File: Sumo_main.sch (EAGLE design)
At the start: 52 parts, among them IC1 TL331, U1 ATMEGA8U2AU, U2 SN65HVD3082, U3 LM339D, X2 RS485, Y1 16MHz

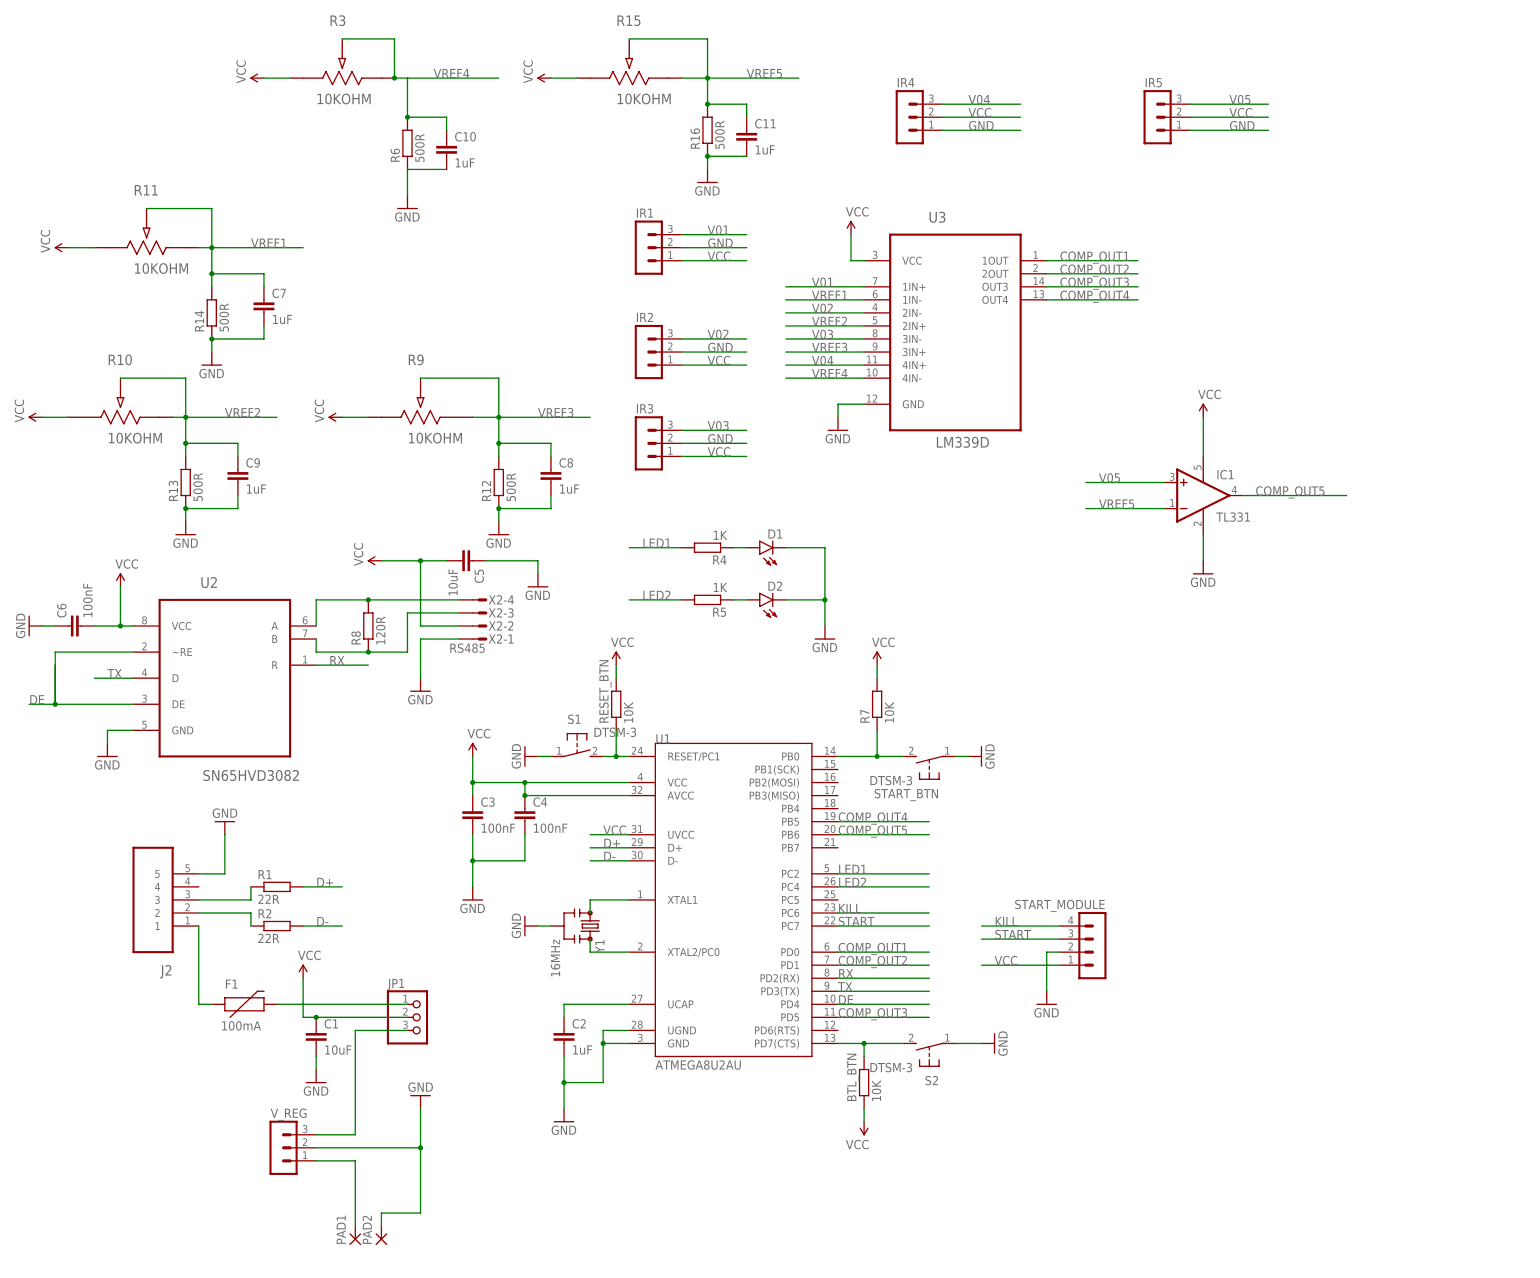
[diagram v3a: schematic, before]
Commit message: Add line sensor to schematic.
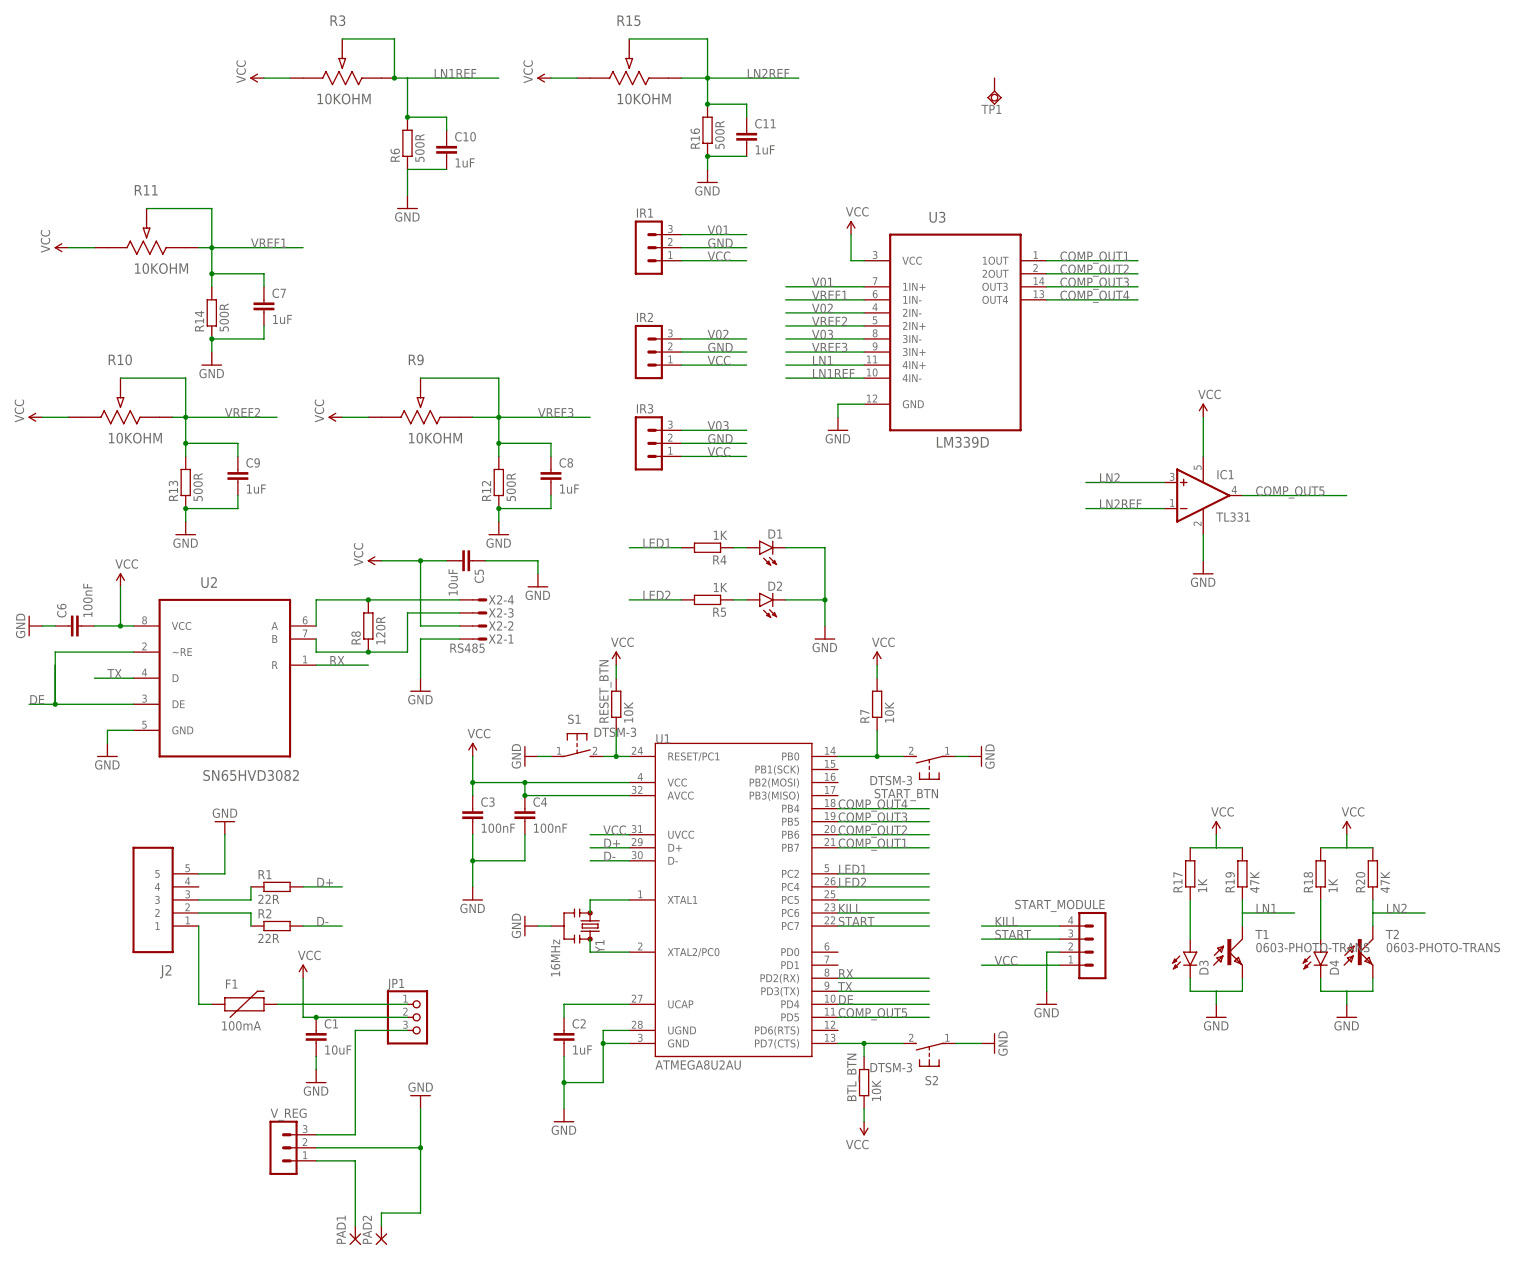
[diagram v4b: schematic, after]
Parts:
- removed IR4, IR5: (no value), con-lstb:MA03-1
- added D3, D4: (no value), SparkFun-LED:LED0603
- added R17, R18: 1K, resistor:R-EU_R0603
- added R19, R20: 47K, resistor:R-EU_R0603
- added T1, T2: 0603-PHOTO-TRANS, Phototransistor 0603:0603-PHOTO-TRANS
- added TP1: TPSQTP08SQ, testpad:TPSQTP08SQ
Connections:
- net VREF4 renamed LN1REF
- net VREF5 renamed LN2REF
- removed net V04: IR4.3, U3.4IN+
- removed net V05: IC1.+IN, IR5.3
- new net LN1: R19.1, T1.C, U3.4IN+
- new net LN2: IC1.+IN, R20.1, T2.C
- new net N$15: D3.A, R17.1
- new net N$17: U1.PC5
- new net N$18: D4.A, R18.1
- net COMP_OUT1: now also U1.PB7; no longer U1.PD0
- net COMP_OUT2: now also U1.PB6; no longer U1.PD1
- net COMP_OUT3: now also U1.PB5; no longer U1.PD5
- net COMP_OUT4: now also U1.PB4; no longer U1.PB5
- net COMP_OUT5: now also U1.PD5; no longer U1.PB6
- net GND: now also D3.C, D4.C, IR2.2, T1.E, T2.E; no longer IR4.1, IR5.1
- net VCC: now also R17.2, R18.2, R19.2, R20.2; no longer IR4.2, IR5.2

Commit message: Remove unnecessary components that are moved to other board.
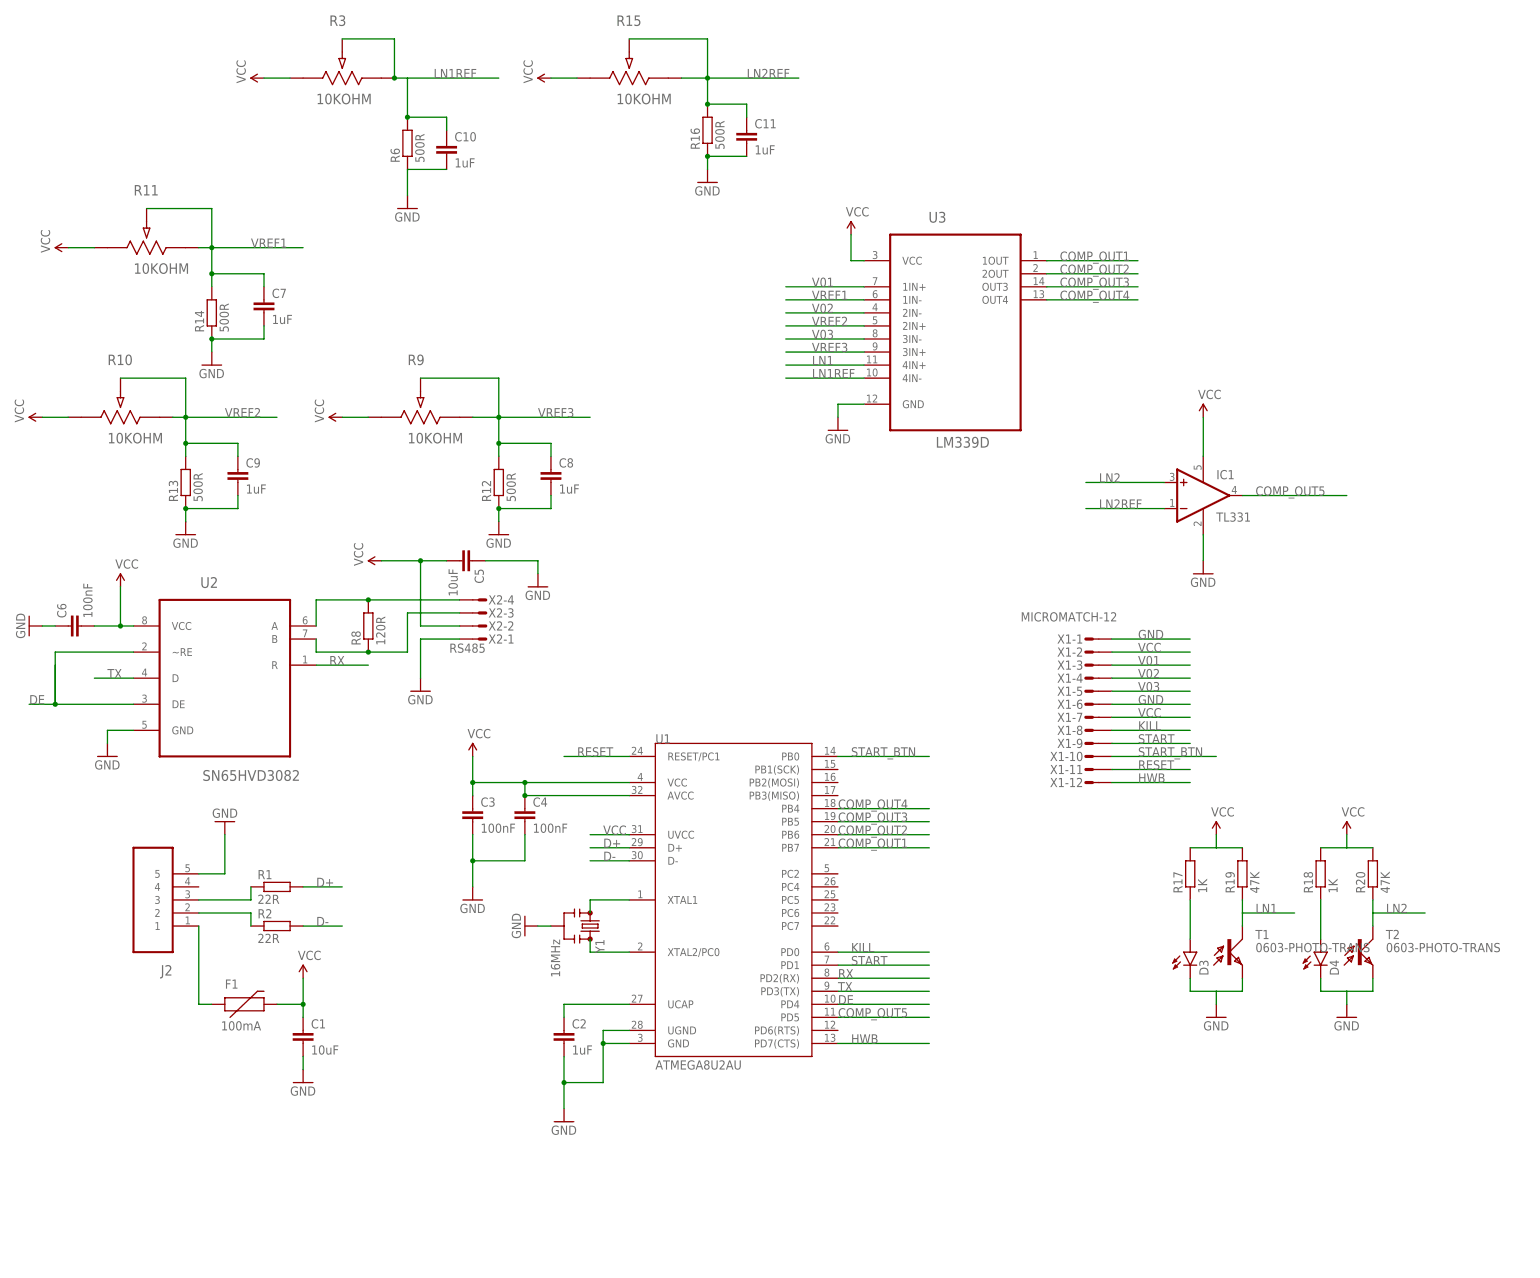
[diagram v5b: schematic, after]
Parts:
- removed BTL_BTN, R7, RESET_BTN: 10K, resistor:R-EU_R0603
- removed D1, D2: (no value), SparkFun-LED:LED0603
- removed IR1, IR2, IR3, V_REG: (no value), con-lstb:MA03-1
- removed JP1: (no value), pinhead:PINHD-1X3
- removed PAD1, PAD2: (no value), wirepad:2,15/1,0
- removed R4, R5: 1K, resistor:R-EU_R0603
- removed S1, S2, START_BTN: DTSM-3, switch-tact:DTSM-3
- removed START_MODULE: (no value), con-lstb:MA04-1
- removed TP1: TPSQTP08SQ, testpad:TPSQTP08SQ
- added X1: MICROMATCH-12, con-amp-micromatch:MICROMATCH-12
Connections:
- removed net LED1: R4.2, U1.PC2
- removed net LED2: R5.2, U1.PC4
- removed net N$10: D1.A, R4.1
- removed net N$12: F1.2, JP1.1
- removed net N$13: BTL_BTN.2, S2.2, U1.PD7(CTS)
- removed net N$14: JP1.3, V_REG.3
- removed net N$17: U1.PC5
- removed net N$23: PAD1.P, V_REG.1
- removed net N$4: RESET_BTN.1, S1.2, U1.RESET/PC1
- removed net N$8: R7.1, START_BTN.2, U1.PB0
- removed net N$9: D2.A, R5.1
- new net HWB: U1.PD7(CTS), X1-12.S
- new net RESET: U1.RESET/PC1, X1-11.S
- new net START_BTN: U1.PB0, X1-10.S
- net GND: now also X1-1.S, X1-6.S; no longer D1.C, D2.C, IR1.2, IR2.2, IR3.2, PAD2.P, S1.1, S2.1, START_BTN.1, START_MODULE.2, V_REG.2
- net KILL: now also U1.PD0, X1-8.S; no longer START_MODULE.4, U1.PC6
- net START: now also U1.PD1, X1-9.S; no longer START_MODULE.3, U1.PC7
- net V01: now also X1-3.S; no longer IR1.3
- net V02: now also X1-4.S; no longer IR2.3
- net V03: now also X1-5.S; no longer IR3.3
- net VCC: now also F1.2, X1-2.S, X1-7.S; no longer BTL_BTN.1, IR1.1, IR2.1, IR3.1, JP1.2, R7.2, RESET_BTN.2, START_MODULE.1
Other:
- moved on the sheet: C1

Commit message: Finish and fix errors of Main's schematic and board
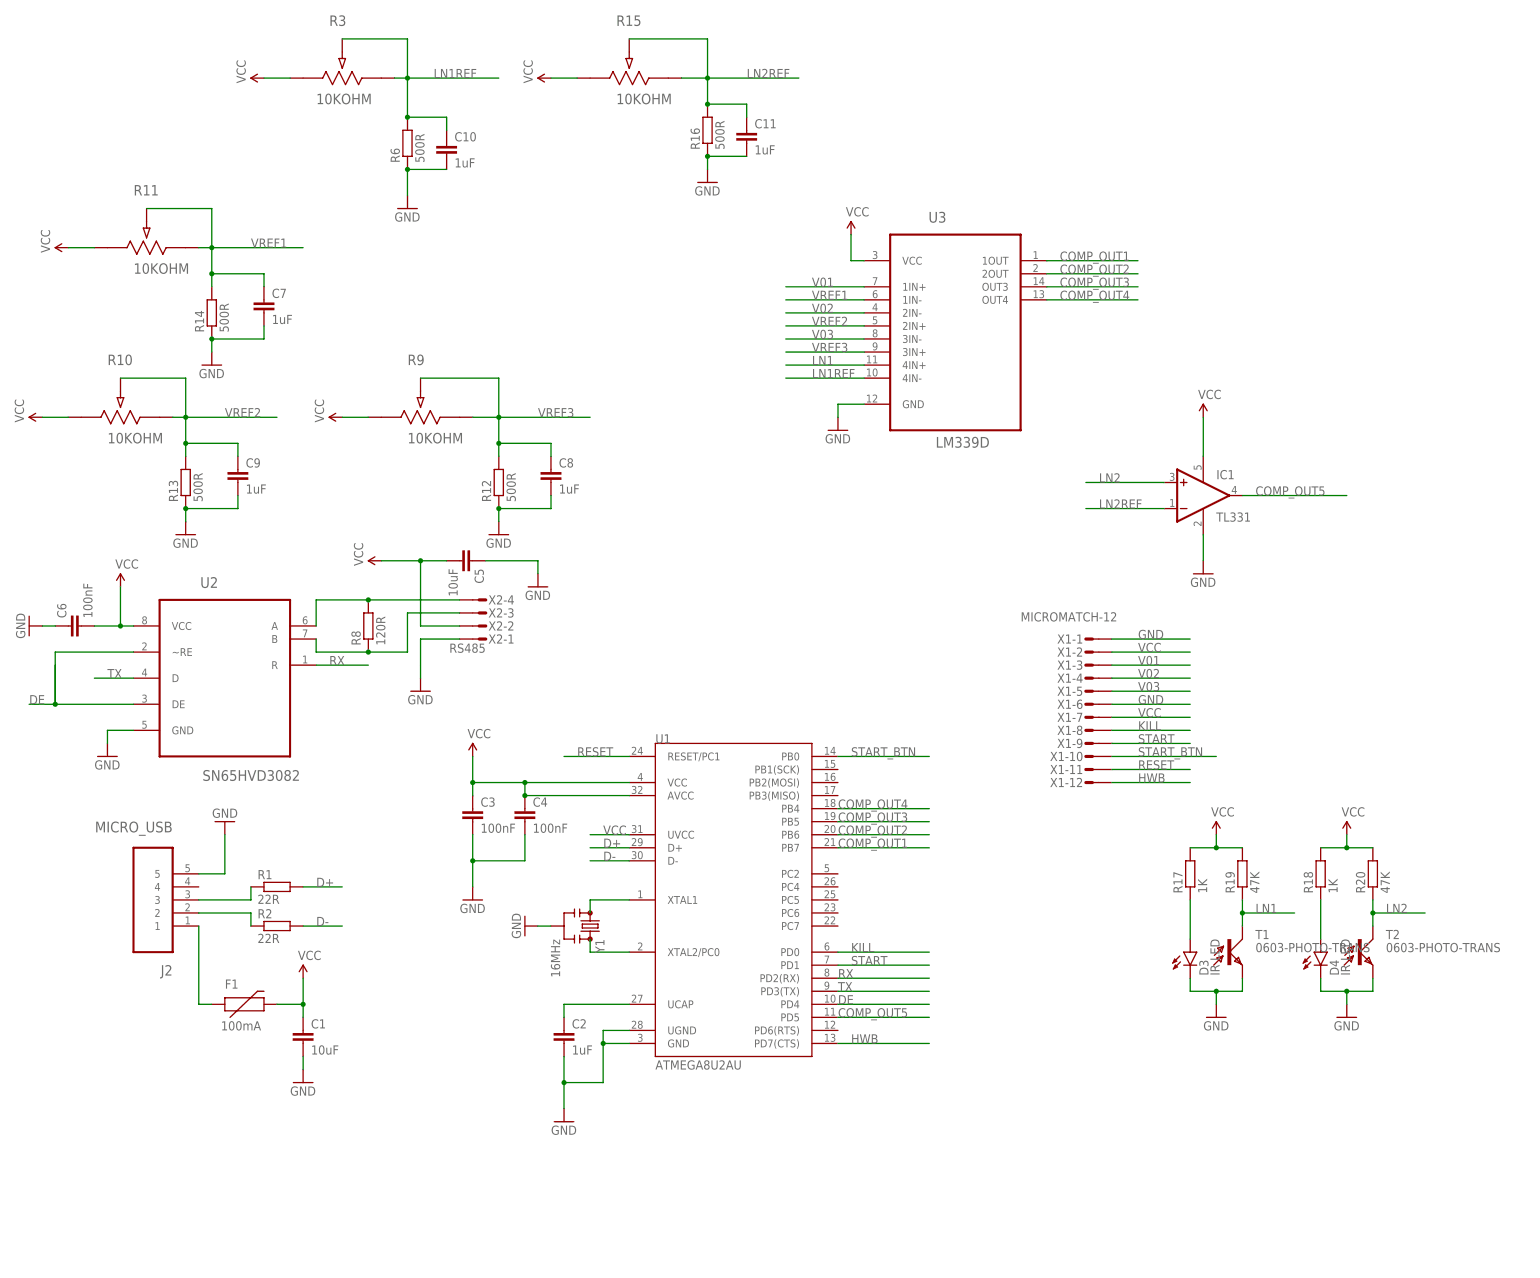
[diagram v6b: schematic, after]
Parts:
- D3, D4: value (none) -> IR LED
- J2: value (none) -> MICRO_USB
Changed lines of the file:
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@@
 <part name="GND17" library="SparkFun-Aesthetics" deviceset="GND" device=""/>
 <part name="GND18" library="SparkFun-Aesthetics" deviceset="GND" device=""/>
-<part name="J2" library="Molex-47346-0001" deviceset="47346-0001" device=""/>
+<part name="J2" library="Molex-47346-0001" deviceset="47346-0001" device="" value="MICRO_USB"/>
 <part name="R3" library="Panasonic-Trimmer_Potentiometers" deviceset="EVM" device="-3W" technology="3YSX50B14" value=" 10KOHM "/>
 <part name="R6" library="resistor" deviceset="R-EU_" device="R0603" value="500R"/>
@@
 <part name="R17" library="resistor" deviceset="R-EU_" device="R0603" value="1K"/>
 <part name="R18" library="resistor" deviceset="R-EU_" device="R0603" value="1K"/>
-<part name="D3" library="SparkFun-LED" deviceset="LED" device="0603"/>
-<part name="D4" library="SparkFun-LED" deviceset="LED" device="0603"/>
+<part name="D3" library="SparkFun-LED" deviceset="LED" device="0603" value="IR LED"/>
+<part name="D4" library="SparkFun-LED" deviceset="LED" device="0603" value="IR LED"/>
 <part name="R19" library="resistor" deviceset="R-EU_" device="R0603" value="47K"/>
 <part name="R20" library="resistor" deviceset="R-EU_" device="R0603" value="47K"/>
@@
 <wire x1="172.72" y1="68.58" x2="167.64" y2="68.58" width="0.1524" layer="91"/>
 <pinref part="SUPPLY15" gate="G$1" pin="VCC"/>
+<junction x="167.64" y="68.58"/>
 </segment>
 <segment>
@@
 <wire x1="198.12" y1="68.58" x2="193.04" y2="68.58" width="0.1524" layer="91"/>
 <pinref part="SUPPLY16" gate="G$1" pin="VCC"/>
+<junction x="193.04" y="68.58"/>
 </segment>
 <segment>
@@
 <pinref part="C10" gate="G$1" pin="2"/>
 <wire x1="17.78" y1="200.66" x2="10.16" y2="200.66" width="0.1524" layer="91"/>
+<junction x="10.16" y="200.66"/>
 </segment>
 <segment>
@@
 <wire x1="167.64" y1="40.64" x2="167.64" y2="38.1" width="0.1524" layer="91"/>
 <pinref part="GND23" gate="1" pin="GND"/>
+<junction x="167.64" y="40.64"/>
 </segment>
 <segment>
@@
 <wire x1="193.04" y1="40.64" x2="193.04" y2="38.1" width="0.1524" layer="91"/>
 <pinref part="GND24" gate="1" pin="GND"/>
+<junction x="193.04" y="40.64"/>
 </segment>
 <segment>
@@
 <wire x1="198.12" y1="55.88" x2="208.28" y2="55.88" width="0.1524" layer="91"/>
 <label x="200.66" y="55.88" size="1.778" layer="95"/>
+<junction x="198.12" y="55.88"/>
 </segment>
 <segment>
@@
 <wire x1="172.72" y1="55.88" x2="182.88" y2="55.88" width="0.1524" layer="91"/>
 <label x="175.26" y="55.88" size="1.778" layer="95"/>
+<junction x="172.72" y="55.88"/>
 </segment>
 </net>
@@
 </segment>
 <segment>
-<pinref part="R3" gate="A" pin="3"/>
-<wire x1="7.62" y1="218.44" x2="10.16" y2="218.44" width="0.1524" layer="91"/>
 <pinref part="R6" gate="G$1" pin="2"/>
 <wire x1="10.16" y1="218.44" x2="10.16" y2="210.82" width="0.1524" layer="91"/>
@@
 <wire x1="17.78" y1="208.28" x2="17.78" y2="210.82" width="0.1524" layer="91"/>
 <wire x1="17.78" y1="210.82" x2="10.16" y2="210.82" width="0.1524" layer="91"/>
-<pinref part="R3" gate="A" pin="2"/>
-<wire x1="7.62" y1="218.44" x2="7.62" y2="226.06" width="0.1524" layer="91"/>
-<wire x1="7.62" y1="226.06" x2="-2.54" y2="226.06" width="0.1524" layer="91"/>
-<junction x="7.62" y="218.44"/>
 <junction x="10.16" y="210.82"/>
 <wire x1="10.16" y1="218.44" x2="27.94" y2="218.44" width="0.1524" layer="91"/>
 <label x="15.24" y="218.44" size="1.778" layer="95"/>
+<pinref part="R3" gate="A" pin="3"/>
+<wire x1="7.62" y1="218.44" x2="10.16" y2="218.44" width="0.1524" layer="91"/>
+<pinref part="R3" gate="A" pin="2"/>
+<wire x1="10.16" y1="226.06" x2="-2.54" y2="226.06" width="0.1524" layer="91"/>
+<wire x1="10.16" y1="218.44" x2="10.16" y2="226.06" width="0.1524" layer="91"/>
+<junction x="10.16" y="218.44"/>
 </segment>
 </net>
@@
 </sheet>
 </sheets>
+<errors>
+</errors>
 </schematic>
 </drawing>
